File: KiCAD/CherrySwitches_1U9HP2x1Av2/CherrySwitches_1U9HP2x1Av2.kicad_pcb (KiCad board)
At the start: 2 copper layers, 45.4 x 39.7 mm, 6 parts, among them SW1 SW_SPST_MOUNT, SW2 SW_SPST_MOUNT

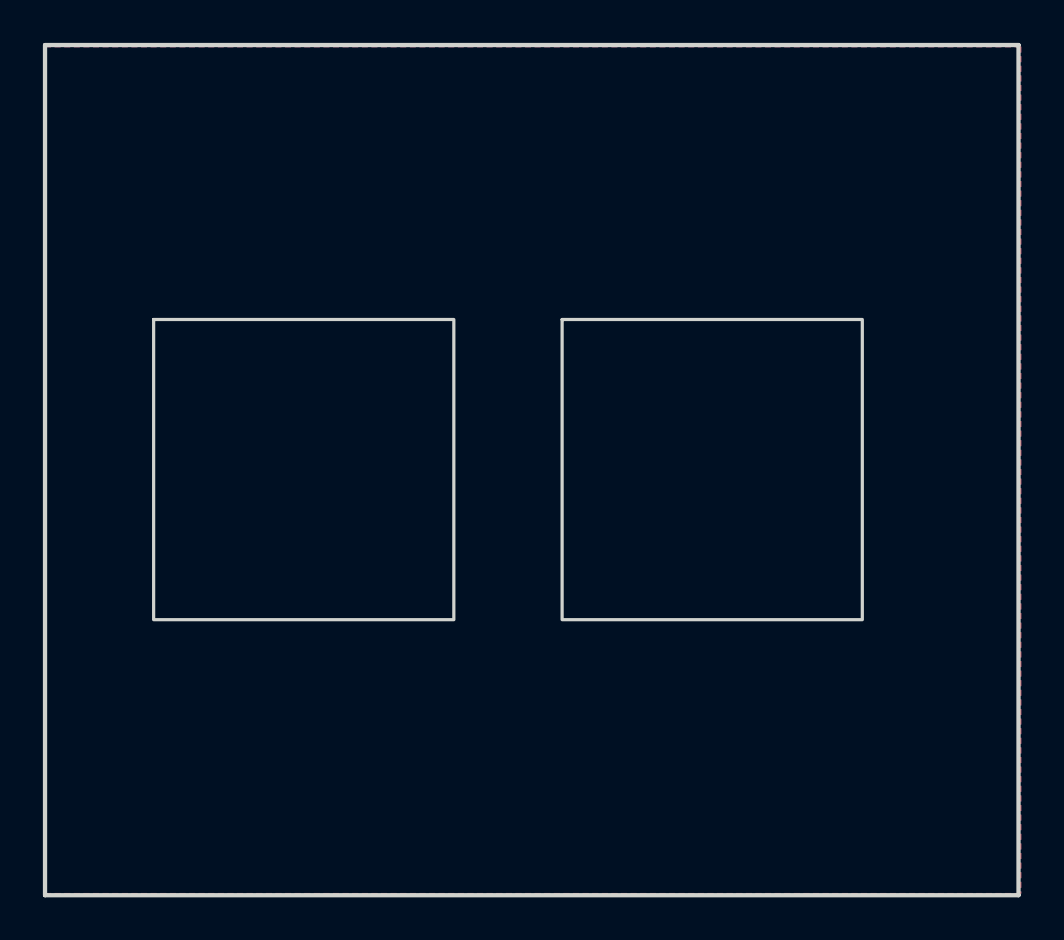
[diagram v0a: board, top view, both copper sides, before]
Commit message: updated all modules to use plated through-holes wherever possible
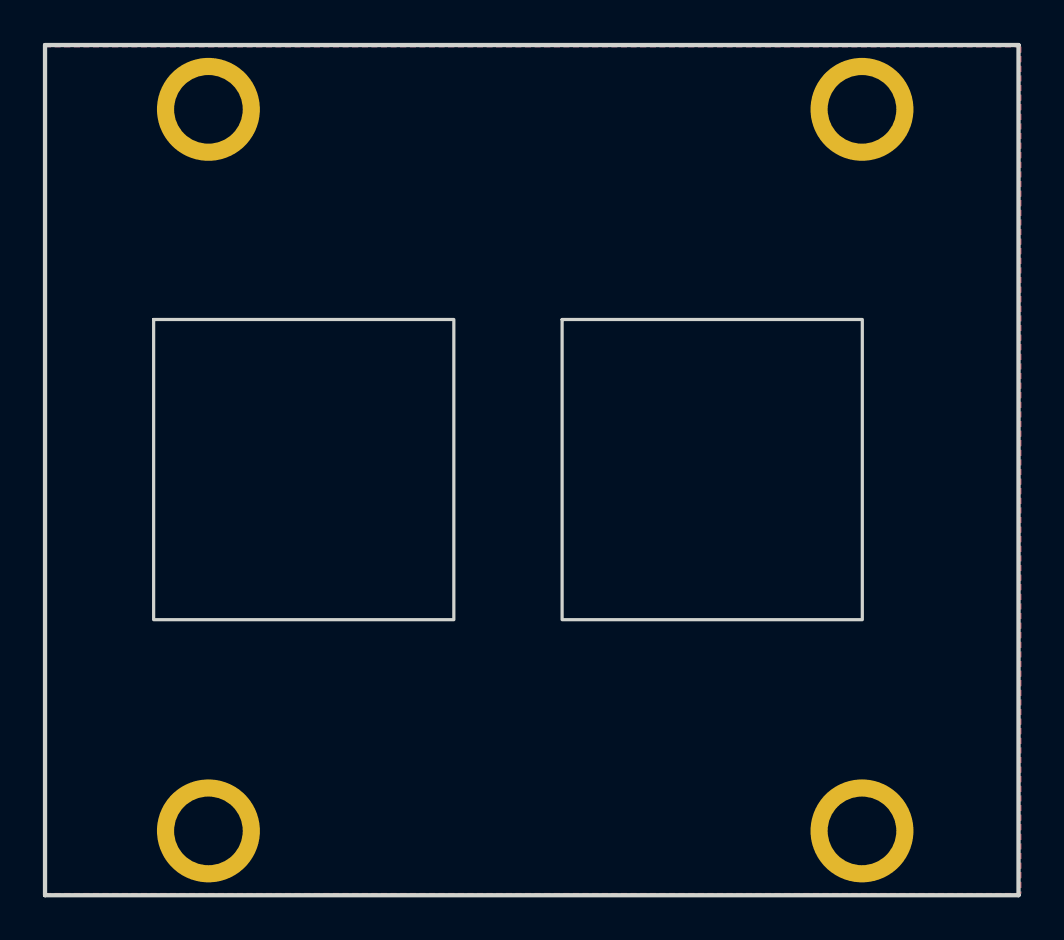
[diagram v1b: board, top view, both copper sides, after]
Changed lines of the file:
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@@
 			)
 		)
-		(pad "" np_thru_hole oval
+		(pad "" thru_hole circle
 			(at 0 0)
-			(size 4.34 3.2)
-			(drill oval 4.34 3.2)
+			(size 4.8 4.8)
+			(drill 3.2)
 			(layers "*.Cu" "*.Mask")
+			(remove_unused_layers no)
 		)
 		(embedded_fonts no)
@@
 			)
 		)
-		(pad "" np_thru_hole oval
+		(pad "" thru_hole circle
 			(at 0 0)
-			(size 4.34 3.2)
-			(drill oval 4.34 3.2)
+			(size 4.8 4.8)
+			(drill 3.2)
 			(layers "*.Cu" "*.Mask")
+			(remove_unused_layers no)
 		)
 		(embedded_fonts no)
@@
 			)
 		)
-		(pad "" np_thru_hole oval
+		(pad "" thru_hole circle
 			(at 0 0)
-			(size 4.34 3.2)
-			(drill oval 4.34 3.2)
+			(size 4.8 4.8)
+			(drill 3.2)
 			(layers "*.Cu" "*.Mask")
+			(remove_unused_layers no)
 		)
 		(embedded_fonts no)
@@
 			)
 		)
-		(pad "" np_thru_hole oval
+		(pad "" thru_hole circle
 			(at 0 0)
-			(size 4.34 3.2)
-			(drill oval 4.34 3.2)
+			(size 4.8 4.8)
+			(drill 3.2)
 			(layers "*.Cu" "*.Mask")
+			(remove_unused_layers no)
 		)
 		(embedded_fonts no)
@@
 			(font
 				(size 1 1)
-				(thickness 0.2)
-				(bold yes)
+				(thickness 0.1)
 			)
 			(justify left bottom mirror)
